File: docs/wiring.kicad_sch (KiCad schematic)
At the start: 14 parts, among them J1 M12 Socket, J16 TowerLight, J18 Barrel Jack, J2 M12 Pin, J3 M12 Socket, J4 M12 Socket, J5 M12 Socket, J6 M12 Pin, J7 M12 Socket, K1 Phoenix 2908215, K2 Relay_SPDT, K3 Phoenix 2908215, K4 Relay_SPDT, K6 Relay_SPDT

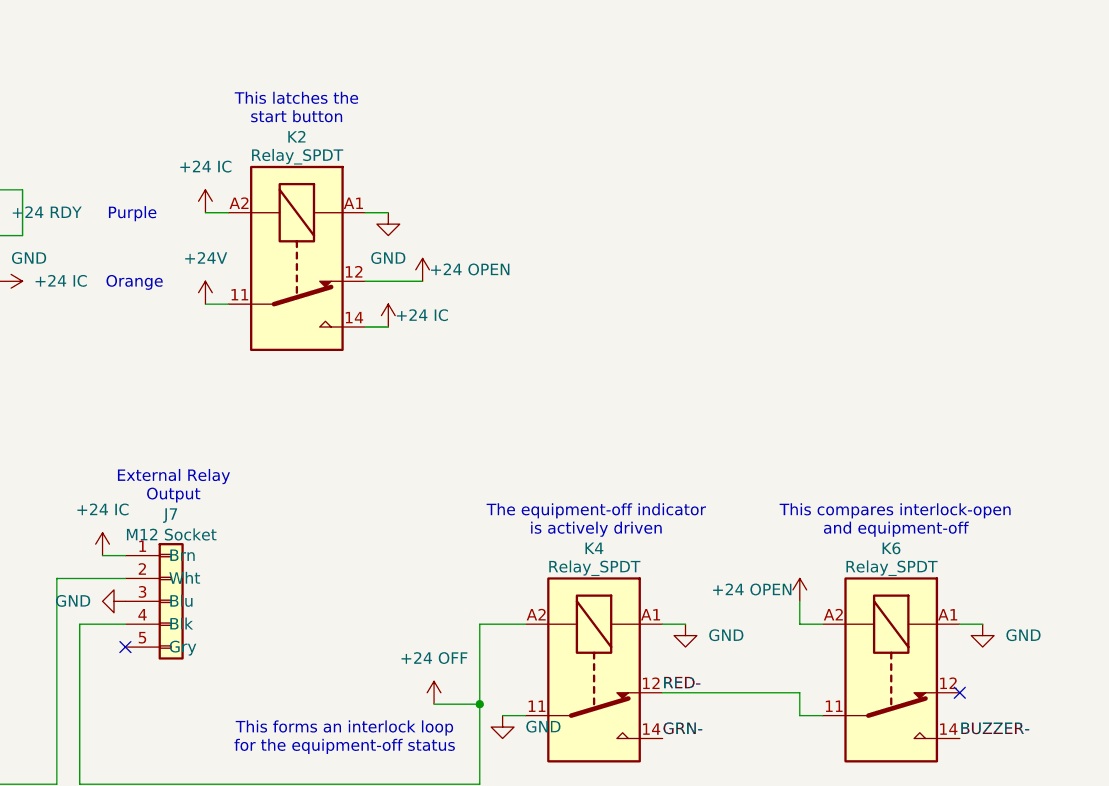
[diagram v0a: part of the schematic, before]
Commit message: corrected wiring diagram
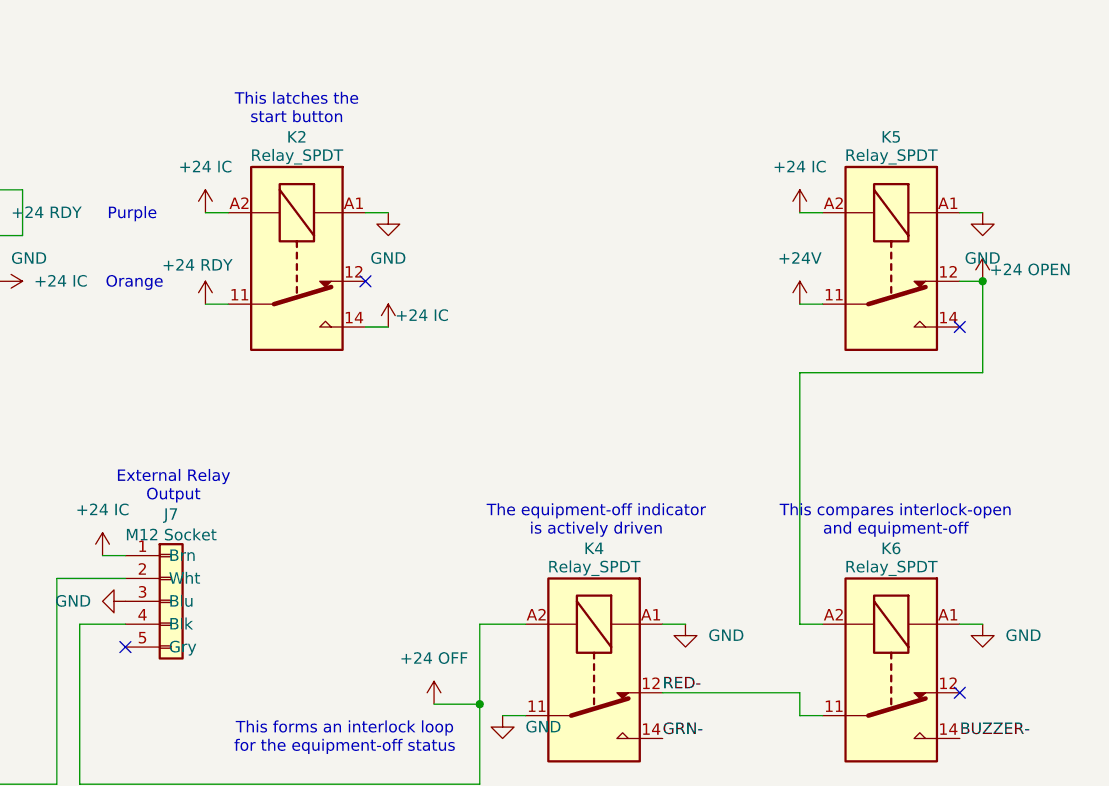
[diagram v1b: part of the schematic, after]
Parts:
- added K5: Relay_SPDT, symbol Relay:Relay_SPDT
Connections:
- net +24 IC: now also K5.A2
- net +24 OPEN: now also K5.12; no longer K2.12
- net +24 RDY: now also K2.11
- net +24V: now also K5.11; no longer K2.11
- net GND: now also K5.A1
- no-connect marks 14 -> 16

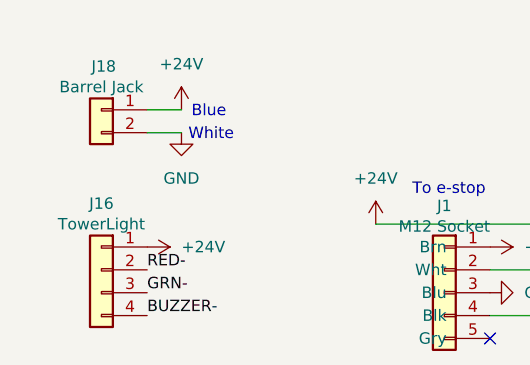
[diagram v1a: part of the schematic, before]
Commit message: update schematic w/ barrel jack sym
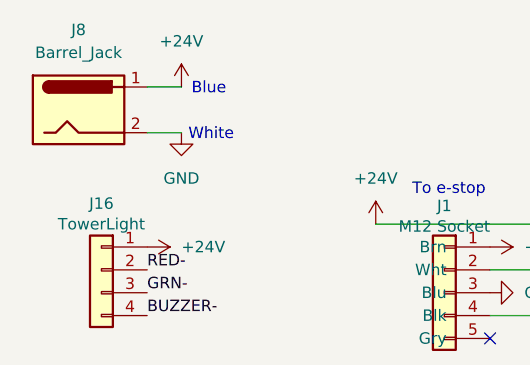
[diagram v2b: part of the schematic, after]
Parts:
- removed J18: Barrel Jack, symbol Connector_Generic:Conn_01x02
- added J8: Barrel_Jack, symbol Connector:Barrel_Jack
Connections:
- net +24V: now also J8.1
- net GND: now also J8.2
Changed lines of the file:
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@@
 	(text "Blue"
 		(exclude_from_sim no)
-		(at 32.258 35.814 0)
+		(at 32.258 33.274 0)
 		(effects
 			(font
@@
 	(wire
 		(pts
-			(xy 25.4 35.56) (xy 29.21 35.56)
+			(xy 25.4 33.02) (xy 29.21 33.02)
 		)
 		(stroke
@@
 	(symbol
 		(lib_id "power:+24V")
-		(at 29.21 35.56 0)
+		(at 29.21 33.02 0)
 		(unit 1)
 		(body_style 1)
@@
 		(fields_autoplaced yes)
 		(property "Reference" "#PWR01"
-			(at 29.21 39.37 0)
+			(at 29.21 36.83 0)
 			(hide yes)
 			(show_name no)
@@
 		)
 		(property "Value" "+24V"
-			(at 29.21 30.48 0)
+			(at 29.21 27.94 0)
 			(show_name no)
 			(do_not_autoplace no)
@@
 		)
 		(property "Footprint" ""
-			(at 29.21 35.56 0)
+			(at 29.21 33.02 0)
 			(hide yes)
 			(show_name no)
@@
 		)
 		(property "Datasheet" ""
-			(at 29.21 35.56 0)
+			(at 29.21 33.02 0)
 			(hide yes)
 			(show_name no)
@@
 		)
 		(property "Description" "Power symbol creates a global label with name \"+24V\""
-			(at 29.21 35.56 0)
+			(at 29.21 33.02 0)
 			(hide yes)
 			(show_name no)
@@
 	)
 	(symbol
+		(lib_id "Connector:Barrel_Jack")
+		(at 17.78 35.56 0)
+		(unit 1)
+		(body_style 1)
+		(exclude_from_sim no)
+		(in_bom yes)
+		(on_board yes)
+		(in_pos_files yes)
+		(dnp no)
+		(fields_autoplaced yes)
+		(property "Reference" "J8"
+			(at 17.78 26.67 0)
+			(show_name no)
+			(do_not_autoplace no)
+			(effects
+				(font
+					(size 1.27 1.27)
+				)
+			)
+		)
+		(property "Value" "Barrel_Jack"
+			(at 17.78 29.21 0)
+			(show_name no)
+			(do_not_autoplace no)
+			(effects
+				(font
+					(size 1.27 1.27)
+				)
+			)
+		)
+		(property "Footprint" ""
+			(at 19.05 36.576 0)
+			(hide yes)
+			(show_name no)
+			(do_not_autoplace no)
+			(effects
+				(font
+					(size 1.27 1.27)
+				)
+			)
+		)
+		(property "Datasheet" ""
+			(at 19.05 36.576 0)
+			(hide yes)
+			(show_name no)
+			(do_not_autoplace no)
+			(effects
+				(font
+					(size 1.27 1.27)
+				)
+			)
+		)
+		(property "Description" "DC Barrel Jack"
+			(at 17.78 35.56 0)
+			(hide yes)
+			(show_name no)
+			(do_not_autoplace no)
+			(effects
+				(font
+					(size 1.27 1.27)
+				)
+			)
+		)
+		(pin "2"
+		)
+		(pin "1"
+		)
+		(instances
+			(project "wiring"
+				(path "/1ff6de51-8261-4e18-9b9b-4dc4524223f8"
+					(reference "J8")
+					(unit 1)
+				)
+			)
+		)
+	)
+	(symbol
 		(lib_id "power:+24V")
 		(at 88.9 50.8 270)
@@
 					(unit 1)
 				)
-			)
-		)
-	)
-	(symbol
-		(lib_id "Connector_Generic:Conn_01x02")
-		(at 20.32 35.56 0)
-		(mirror y)
-		(unit 1)
-		(body_style 1)
-		(exclude_from_sim no)
-		(in_bom yes)
-		(on_board yes)
-		(in_pos_files yes)
-		(dnp no)
-		(property "Reference" "J18"
-			(at 20.574 30.734 0)
-			(show_name no)
-			(do_not_autoplace no)
-			(effects
-				(font
-					(size 1.27 1.27)
-				)
-			)
-		)
-		(property "Value" "Barrel Jack"
-			(at 20.32 33.02 0)
-			(show_name no)
-			(do_not_autoplace no)
-			(effects
-				(font
-					(size 1.27 1.27)
-				)
-			)
-		)
-		(property "Footprint" ""
-			(at 20.32 35.56 0)
-			(hide yes)
-			(show_name no)
-			(do_not_autoplace no)
-			(effects
-				(font
-					(size 1.27 1.27)
-				)
-			)
-		)
-		(property "Datasheet" ""
-			(at 20.32 35.56 0)
-			(hide yes)
-			(show_name no)
-			(do_not_autoplace no)
-			(effects
-				(font
-					(size 1.27 1.27)
-				)
-			)
-		)
-		(property "Description" "Generic connector, single row, 01x02, script generated (kicad-library-utils/schlib/autogen/connector/)"
-			(at 20.32 35.56 0)
-			(hide yes)
-			(show_name no)
-			(do_not_autoplace no)
-			(effects
-				(font
-					(size 1.27 1.27)
-				)
-			)
-		)
-		(pin "1"
-		)
-		(pin "2"
-		)
-		(instances
-			(project "wiring"
-				(path "/1ff6de51-8261-4e18-9b9b-4dc4524223f8"
-					(reference "J18")
-					(unit 1)
-				)
